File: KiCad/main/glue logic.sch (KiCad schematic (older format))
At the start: 3 parts, among them U12 27C512, U13 74HC32, U14 74HC245

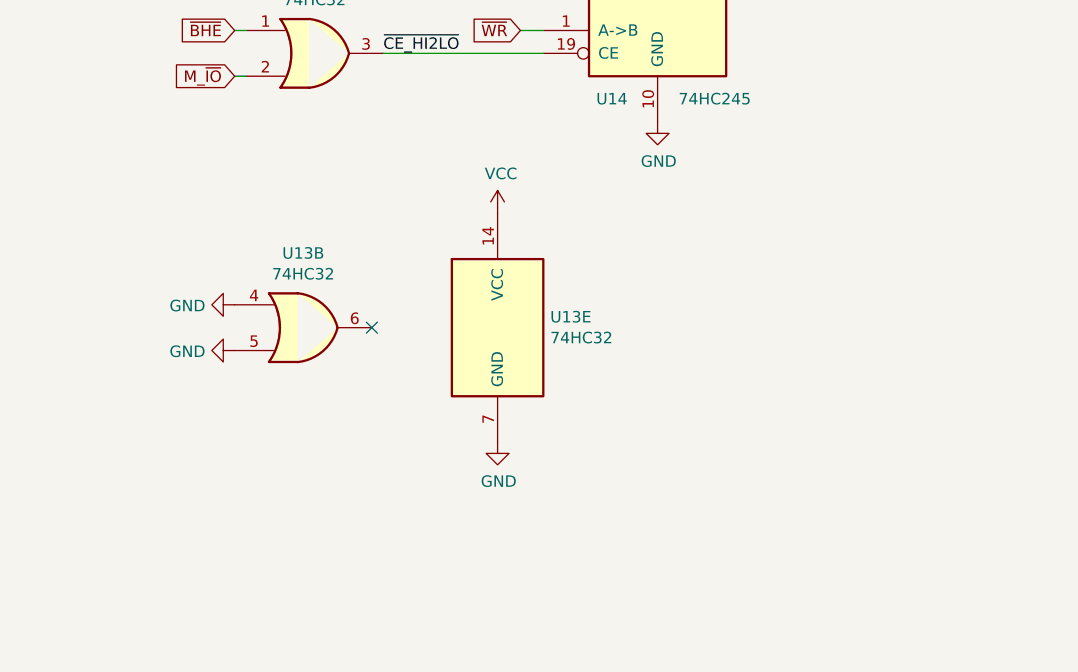
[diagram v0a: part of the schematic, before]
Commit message: Fixed main and info_board bugs.
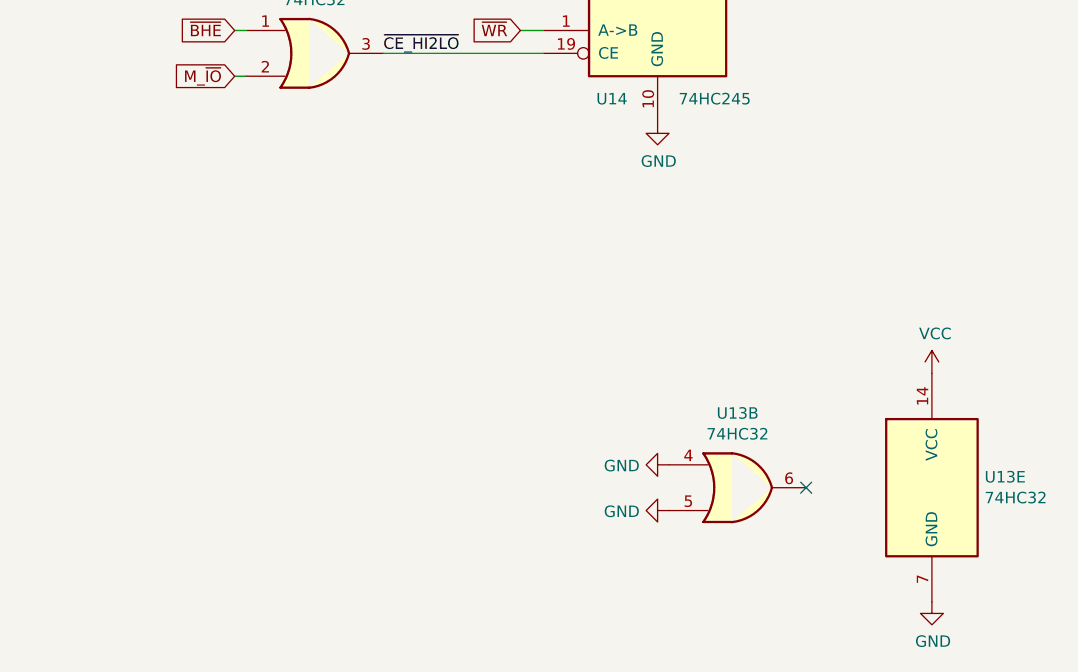
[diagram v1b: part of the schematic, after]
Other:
- moved on the sheet: U13B, U13E
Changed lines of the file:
@@
 L power:GND #PWR061
 U 1 1 5F8ECA6F
-P 6300 4700
-F 0 "#PWR061" H 6300 4450 50  0001 C CNN
-F 1 "GND" V 6305 4572 50  0000 R CNN
-F 2 "" H 6300 4700 50  0001 C CNN
-F 3 "" H 6300 4700 50  0001 C CNN
-	1    6300 4700
+P 8200 5400
+F 0 "#PWR061" H 8200 5150 50  0001 C CNN
+F 1 "GND" V 8205 5272 50  0000 R CNN
+F 2 "" H 8200 5400 50  0001 C CNN
+F 3 "" H 8200 5400 50  0001 C CNN
+	1    8200 5400
 	0    1    1    0
 $EndComp
@@
 L power:GND #PWR0103
 U 1 1 5F9123F3
-P 7450 5100
-F 0 "#PWR0103" H 7450 4850 50  0001 C CNN
-F 1 "GND" H 7455 4927 50  0000 C CNN
-F 2 "" H 7450 5100 50  0001 C CNN
-F 3 "" H 7450 5100 50  0001 C CNN
-	1    7450 5100
+P 9350 5800
+F 0 "#PWR0103" H 9350 5550 50  0001 C CNN
+F 1 "GND" H 9355 5627 50  0000 C CNN
+F 2 "" H 9350 5800 50  0001 C CNN
+F 3 "" H 9350 5800 50  0001 C CNN
+	1    9350 5800
 	1    0    0    -1
 $EndComp
@@
 L power:VCC #PWR0104
 U 1 1 5F912877
-P 7450 4100
-F 0 "#PWR0104" H 7450 3950 50  0001 C CNN
-F 1 "VCC" H 7465 4273 50  0000 C CNN
-F 2 "" H 7450 4100 50  0001 C CNN
-F 3 "" H 7450 4100 50  0001 C CNN
-	1    7450 4100
+P 9350 4800
+F 0 "#PWR0104" H 9350 4650 50  0001 C CNN
+F 1 "VCC" H 9365 4973 50  0000 C CNN
+F 2 "" H 9350 4800 50  0001 C CNN
+F 3 "" H 9350 4800 50  0001 C CNN
+	1    9350 4800
 	1    0    0    -1
 $EndComp
-NoConn ~ 6900 4600
+NoConn ~ 8800 5300
 $Comp
 L power:GND #PWR0107
 U 1 1 5F8CAB2B
-P 6300 4500
-F 0 "#PWR0107" H 6300 4250 50  0001 C CNN
-F 1 "GND" V 6305 4372 50  0000 R CNN
-F 2 "" H 6300 4500 50  0001 C CNN
-F 3 "" H 6300 4500 50  0001 C CNN
-	1    6300 4500
+P 8200 5200
+F 0 "#PWR0107" H 8200 4950 50  0001 C CNN
+F 1 "GND" V 8205 5072 50  0000 R CNN
+F 2 "" H 8200 5200 50  0001 C CNN
+F 3 "" H 8200 5200 50  0001 C CNN
+	1    8200 5200
 	0    1    1    0
 $EndComp
@@
 L 74xx:74LS32 U13
 U 2 1 5F94812C
-P 6600 4600
-F 0 "U13" H 6600 4925 50  0000 C CNN
-F 1 "74HC32" H 6600 4834 50  0000 C CNN
-F 2 "Package_DIP:DIP-14_W7.62mm_LongPads" H 6600 4600 50  0001 C CNN
-F 3 "http://www.ti.com/lit/gpn/sn74LS32" H 6600 4600 50  0001 C CNN
-	2    6600 4600
+P 8500 5300
+F 0 "U13" H 8500 5625 50  0000 C CNN
+F 1 "74HC32" H 8500 5534 50  0000 C CNN
+F 2 "Package_DIP:DIP-14_W7.62mm_LongPads" H 8500 5300 50  0001 C CNN
+F 3 "http://www.ti.com/lit/gpn/sn74LS32" H 8500 5300 50  0001 C CNN
+	2    8500 5300
 	1    0    0    -1
 $EndComp
@@
 L 74xx:74LS32 U13
 U 5 1 5F9490B6
-P 7450 4600
-F 0 "U13" H 7680 4646 50  0000 L CNN
-F 1 "74HC32" H 7680 4555 50  0000 L CNN
-F 2 "Package_DIP:DIP-14_W7.62mm_LongPads" H 7450 4600 50  0001 C CNN
-F 3 "http://www.ti.com/lit/gpn/sn74LS32" H 7450 4600 50  0001 C CNN
-	5    7450 4600
+P 9350 5300
+F 0 "U13" H 9580 5346 50  0000 L CNN
+F 1 "74HC32" H 9580 5255 50  0000 L CNN
+F 2 "Package_DIP:DIP-14_W7.62mm_LongPads" H 9350 5300 50  0001 C CNN
+F 3 "http://www.ti.com/lit/gpn/sn74LS32" H 9350 5300 50  0001 C CNN
+	5    9350 5300
 	1    0    0    -1
 $EndComp
